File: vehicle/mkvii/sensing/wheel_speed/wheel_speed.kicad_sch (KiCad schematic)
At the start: 8 parts, among them U1 ATMEGA16M1, Y1 Crystal_16MHz_18pF

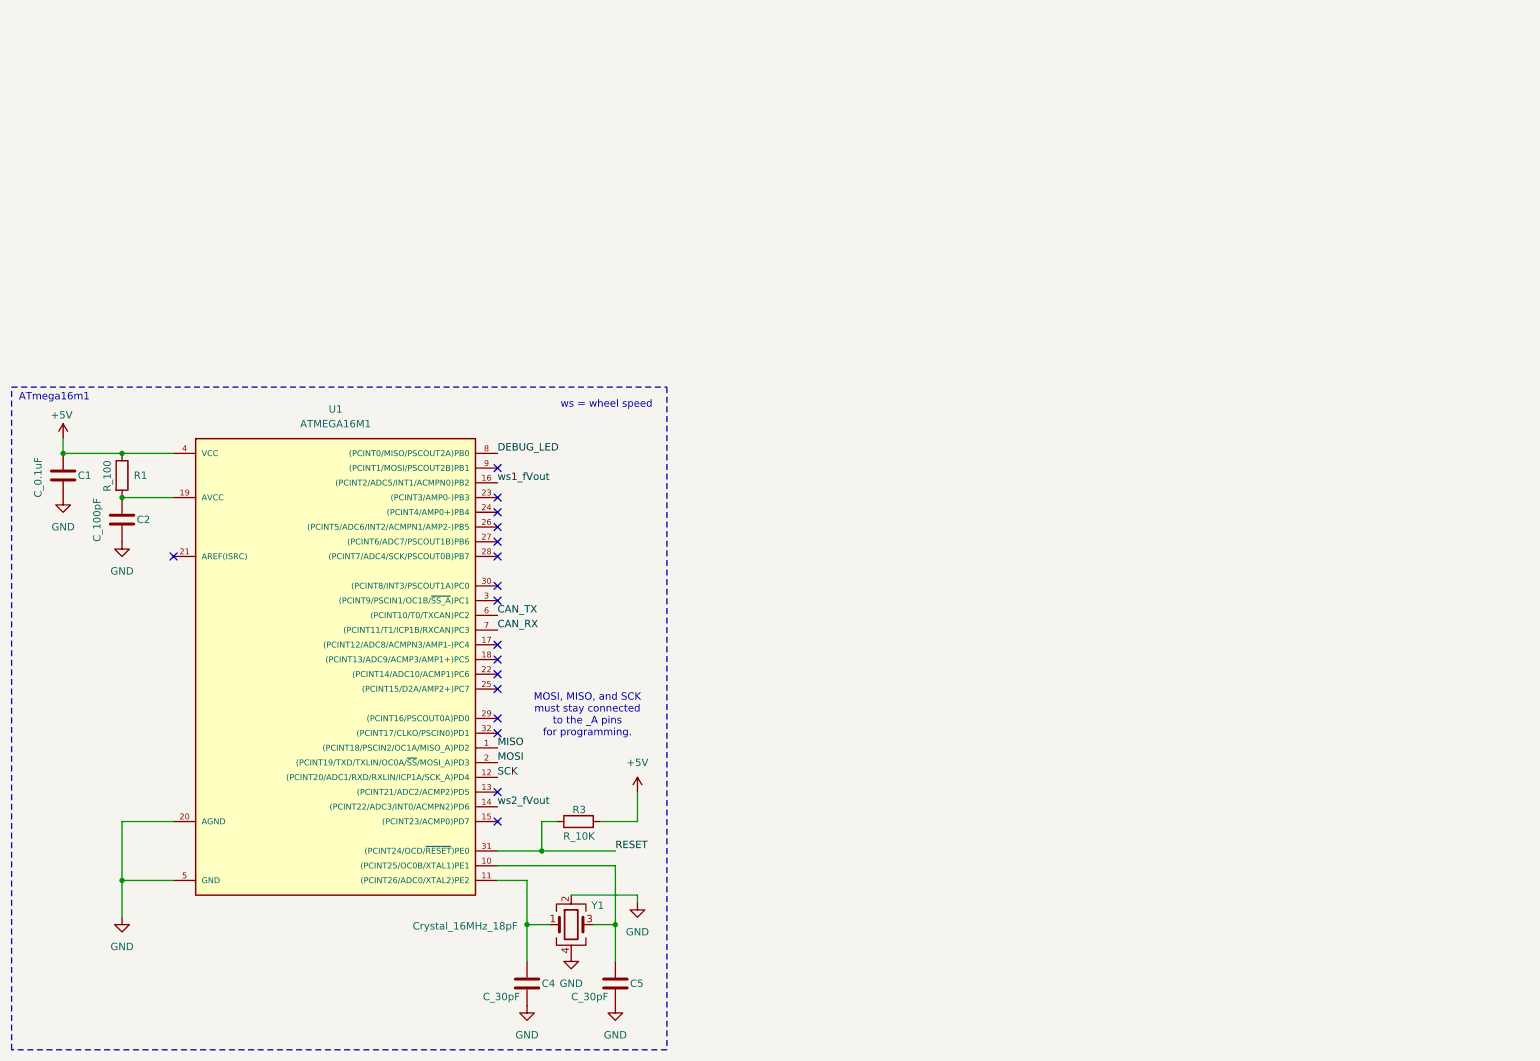
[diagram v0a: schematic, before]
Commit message: Add wheel speed board
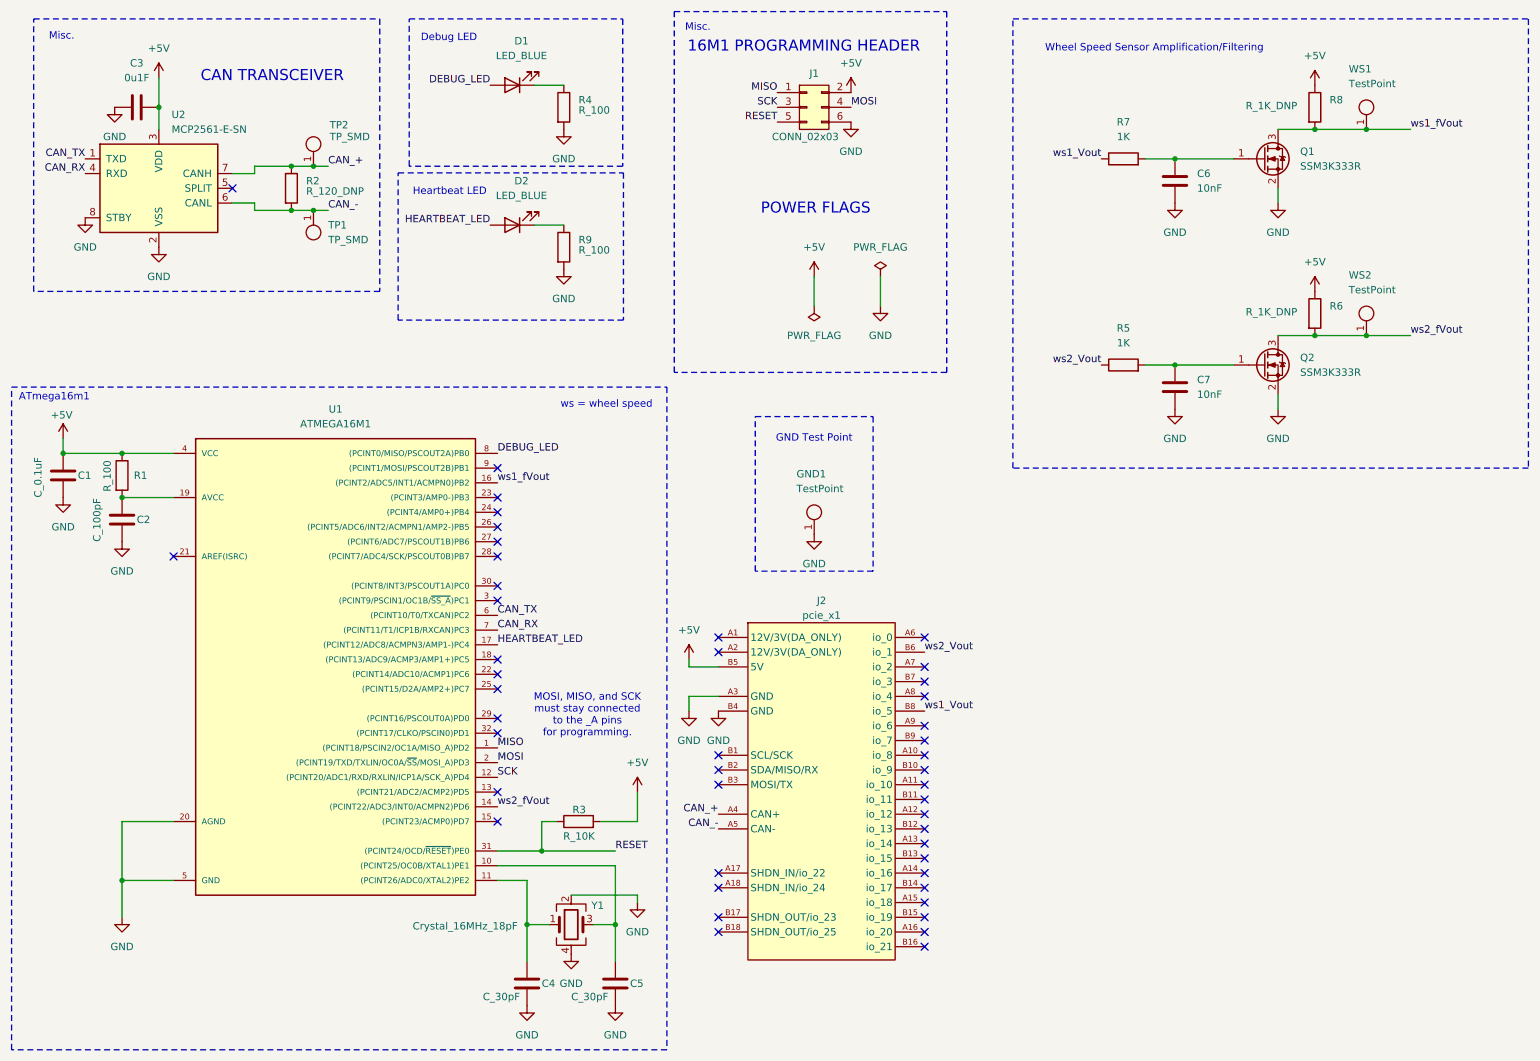
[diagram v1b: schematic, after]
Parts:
- added C3: 0u1F, OEM:C_0603, symbol OEM:0u1F
- added C6, C7: 10nF, OEM:C_0603, symbol OEM:C
- added D1, D2: LED_BLUE, OEM:CHIPLED_0805, symbol OEM:LED_BLUE
- added GND1, WS1, WS2: TestPoint, TestPoint:TestPoint_Pad_D1.0mm, symbol OEM:TP_1mm
- added J1: CONN_02x03, Connector_PinHeader_2.54mm:PinHeader_2x03_P2.54mm_Vertical, symbol OEM:CONN_02x03
- added J2: pcie_x1, OEM:pcie_x1, symbol OEM:pcie_x1
- added Q1, Q2: SSM3K333R, OEM:SOT-23F, symbol OEM:SSM3K333R
- added R2: R_120_DNP, OEM:R_0603, symbol OEM:R
- added R4, R9: R_100, OEM:R_0603, symbol OEM:R
- added R5, R7: 1K, OEM:R_0603, symbol OEM:R
- added R6, R8: R_1K_DNP, OEM:R_0603, symbol OEM:R
- added TP1, TP2: TP_SMD, OEM:Test_Point_SMD, symbol OEM:TP_SMD
- added U2: MCP2561-E-SN, Package_SO:SOIC-8_3.9x4.9mm_P1.27mm, symbol Interface_CAN_LIN:MCP2561-E-SN
- R1, R3: footprint (none) -> OEM:R_0603
- U1: footprint footprints:TQFP-32_7x7mm_Pitch0.8mm -> OEM:TQFP-32_7x7mm_Pitch0.8mm
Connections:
- net +5V: now also C3.2, J1.2 (P2), J2.B5 (5V), R6.1, R8.1, U2.3 (VDD)
- net CAN_RX: now also U2.4 (RXD)
- net CAN_TX: now also U2.1 (TXD)
- net DEBUG_LED: now also D1.2 (A)
- net GND: now also C3.1, C6.2, C7.2, GND1.1, J1.6 (P6), J2.A3 (GND), J2.B4 (GND), Q1.2 (S), Q2.2 (S), R4.2, R9.2, U2.2 (VSS), U2.8 (STBY)
- net MISO: now also J1.1 (P1)
- net MOSI: now also J1.4 (P4)
- net RESET: now also J1.5 (P5)
- net SCK: now also J1.3 (P3)
- net ws1_fVout: now also Q1.3 (D), R8.2, WS1.1
- net ws2_fVout: now also Q2.3 (D), R6.2, WS2.1
- net HEARTBEAT_LED: now reaches U1.17 ((PCINT12/ADC8/ACMPN3/AMP1-)PC4)
- net HEARTBEAT_LED: now also D2.2 (A)
- new net: C6.1, Q1.1 (G), R7.2
- new net: C7.1, Q2.1 (G), R5.2
- new net: D2.1 (K), R9.1
- new net: D1.1 (K), R4.1
- new net CAN_+: J2.A4 (CAN+), R2.1, TP2.1, U2.7 (CANH)
- new net CAN_-: J2.A5 (CAN-), R2.2, TP1.1, U2.6 (CANL)
- new net ws1_Vout: J2.B8 (io_5), R7.1
- new net ws2_Vout: J2.B6 (io_1), R5.1
- no-connect marks 17 -> 46
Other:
- note added: "16M1 PROGRAMMING HEADER"
- note added: "CAN TRANSCEIVER"
- note added: "Debug LED"
- note added: "GND Test Point"
- note added: "Heartbeat LED"
- note added: "Misc."
- note added: "POWER FLAGS"
- note added: "Wheel Speed Sensor Amplification/Filtering"

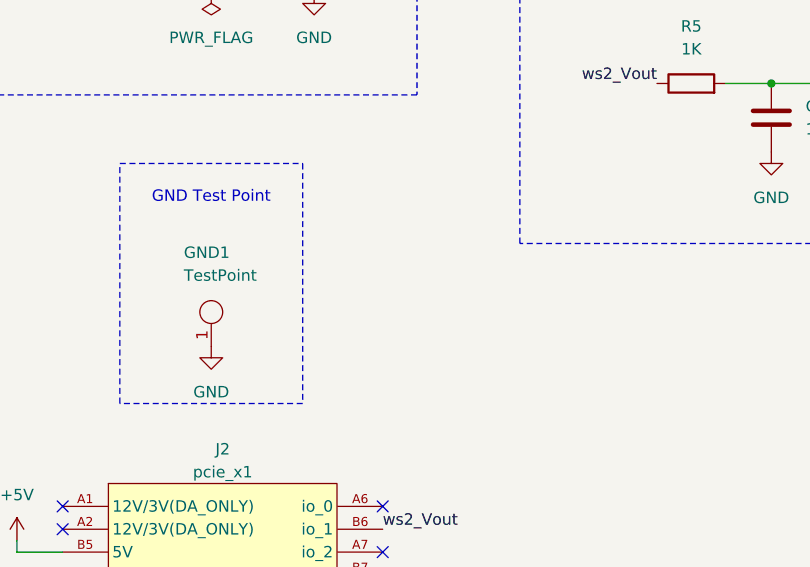
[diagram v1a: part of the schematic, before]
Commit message: Add rounded edges
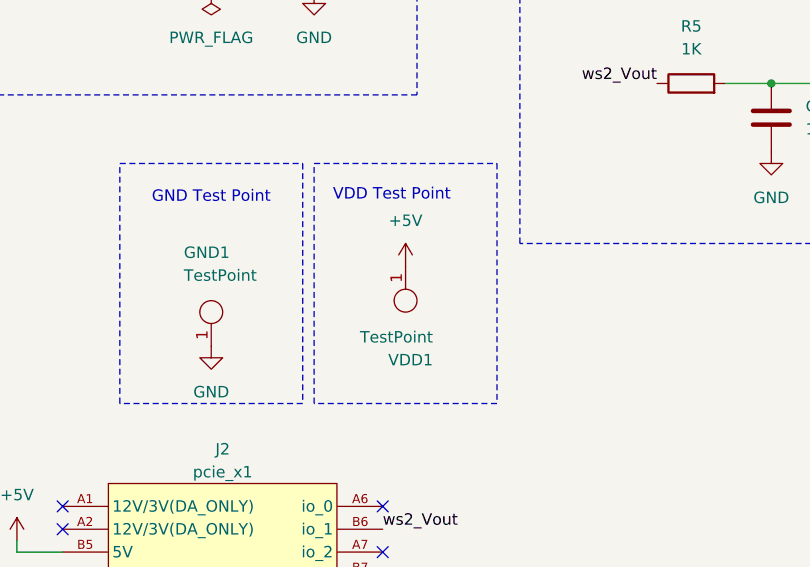
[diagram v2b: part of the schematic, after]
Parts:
- added VDD1: TestPoint, TestPoint:TestPoint_Pad_D1.0mm, symbol OEM:TP_1mm
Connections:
- net +5V: now also VDD1.1
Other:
- note added: "VDD Test Point"
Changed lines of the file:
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@@
 	)
 	(rectangle
+		(start 165.1 85.09)
+		(end 185.42 111.76)
+		(stroke
+			(width 0)
+			(type dash)
+		)
+		(fill
+			(type none)
+		)
+	)
+	(rectangle
 		(start 143.51 85.09)
 		(end 163.83 111.76)
@@
 		)
 	)
+	(text "VDD Test Point"
+		(exclude_from_sim no)
+		(at 173.736 88.646 0)
+		(effects
+			(font
+				(size 1.27 1.27)
+			)
+		)
+	)
 	(text "ATmega16m1"
 		(exclude_from_sim no)
@@
 	)
 	(symbol
+		(lib_id "OEM:TP_1mm")
+		(at 175.26 97.79 180)
+		(unit 1)
+		(exclude_from_sim no)
+		(in_bom no)
+		(on_board yes)
+		(dnp no)
+		(property "Reference" "VDD1"
+			(at 178.308 106.934 0)
+			(effects
+				(font
+					(size 1.27 1.27)
+				)
+				(justify left)
+			)
+		)
+		(property "Value" "TestPoint"
+			(at 178.308 104.394 0)
+			(effects
+				(font
+					(size 1.27 1.27)
+				)
+				(justify left)
+			)
+		)
+		(property "Footprint" "TestPoint:TestPoint_Pad_D1.0mm"
+			(at 175.26 93.98 0)
+			(effects
+				(font
+					(size 1.27 1.27)
+				)
+				(hide yes)
+			)
+		)
+		(property "Datasheet" ""
+			(at 175.26 97.79 0)
+			(effects
+				(font
+					(size 1.27 1.27)
+				)
+				(hide yes)
+			)
+		)
+		(property "Description" "test point circular 1mm"
+			(at 175.26 97.79 0)
+			(effects
+				(font
+					(size 1.27 1.27)
+				)
+				(hide yes)
+			)
+		)
+		(property "MPN" ""
+			(at 175.26 97.79 0)
+			(effects
+				(font
+					(size 1.27 1.27)
+				)
+				(hide yes)
+			)
+		)
+		(property "MFN" ""
+			(at 175.26 97.79 0)
+			(effects
+				(font
+					(size 1.27 1.27)
+				)
+				(hide yes)
+			)
+		)
+		(property "DKPN" ""
+			(at 175.26 97.79 0)
+			(effects
+				(font
+					(size 1.27 1.27)
+				)
+				(hide yes)
+			)
+		)
+		(property "NewDesigns" "YES"
+			(at 175.26 97.79 0)
+			(effects
+				(font
+					(size 1.27 1.27)
+				)
+				(hide yes)
+			)
+		)
+		(property "Stocked" ""
+			(at 175.26 97.79 0)
+			(effects
+				(font
+					(size 1.27 1.27)
+				)
+				(hide yes)
+			)
+		)
+		(property "Package" "Custom"
+			(at 175.26 97.79 0)
+			(effects
+				(font
+					(size 1.27 1.27)
+				)
+				(hide yes)
+			)
+		)
+		(property "Style" "SMD"
+			(at 175.26 97.79 0)
+			(effects
+				(font
+					(size 1.27 1.27)
+				)
+				(hide yes)
+			)
+		)
+		(pin "1"
+		)
+		(instances
+			(project "wheel_speed"
+				(path "/e7195ce3-5a1b-4095-9397-a48b8b9b0612"
+					(reference "VDD1")
+					(unit 1)
+				)
+			)
+		)
+	)
+	(symbol
 		(lib_id "power:+5V")
 		(at 132.08 127 0)
@@
 			(effects
 				(font
+					(size 1.27 1.27)
+				)
+				(hide yes)
+			)
+		)
+		(pin "1"
+		)
+		(instances
+			(project ""
+				(path "/e7195ce3-5a1b-4095-9397-a48b8b9b0612"
+					(reference "#PWR?")
+					(unit 1)
+				)
+			)
+		)
+	)
+	(symbol
+		(lib_id "power:+5V")
+		(at 175.26 96.52 0)
+		(unit 1)
+		(exclude_from_sim no)
+		(in_bom yes)
+		(on_board yes)
+		(dnp no)
+		(fields_autoplaced yes)
+		(property "Reference" "#PWR?"
+			(at 175.26 100.33 0)
+			(effects
+				(font
+					(size 1.27 1.27)
+				)
+				(hide yes)
+			)
+		)
+		(property "Value" "+5V"
+			(at 175.26 91.44 0)
+			(effects
+				(font
+					(size 1.27 1.27)
+				)
+			)
+		)
+		(property "Footprint" ""
+			(at 175.26 96.52 0)
+			(effects
+				(font
+					(size 1.27 1.27)
+				)
+				(hide yes)
+			)
+		)
+		(property "Datasheet" ""
+			(at 175.26 96.52 0)
+			(effects
+				(font
+					(size 1.27 1.27)
+				)
+				(hide yes)
+			)
+		)
+		(property "Description" "Power symbol creates a global label with name \"+5V\""
+			(at 175.26 96.52 0)
+			(effects
+				(font
